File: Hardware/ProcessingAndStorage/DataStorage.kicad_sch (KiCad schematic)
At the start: 10 parts, among them J1 Micro_SD_Card_Det2, U3 LD1117S50TR_SOT223

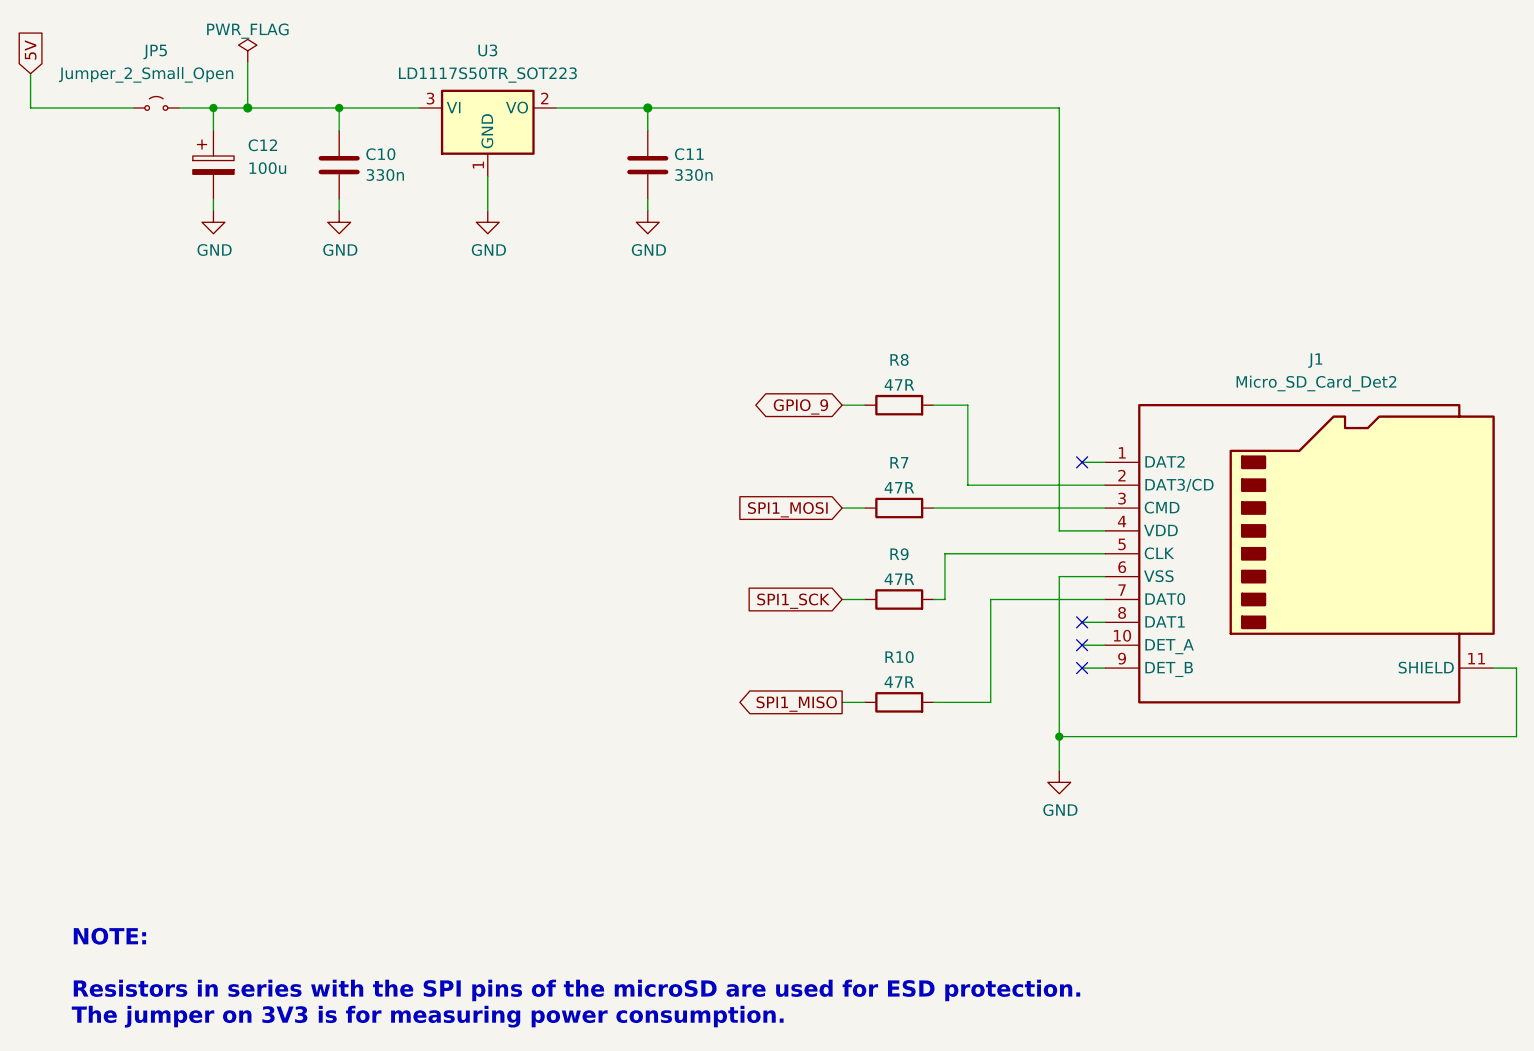
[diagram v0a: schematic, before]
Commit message: make boards smaller, fix sd card slot
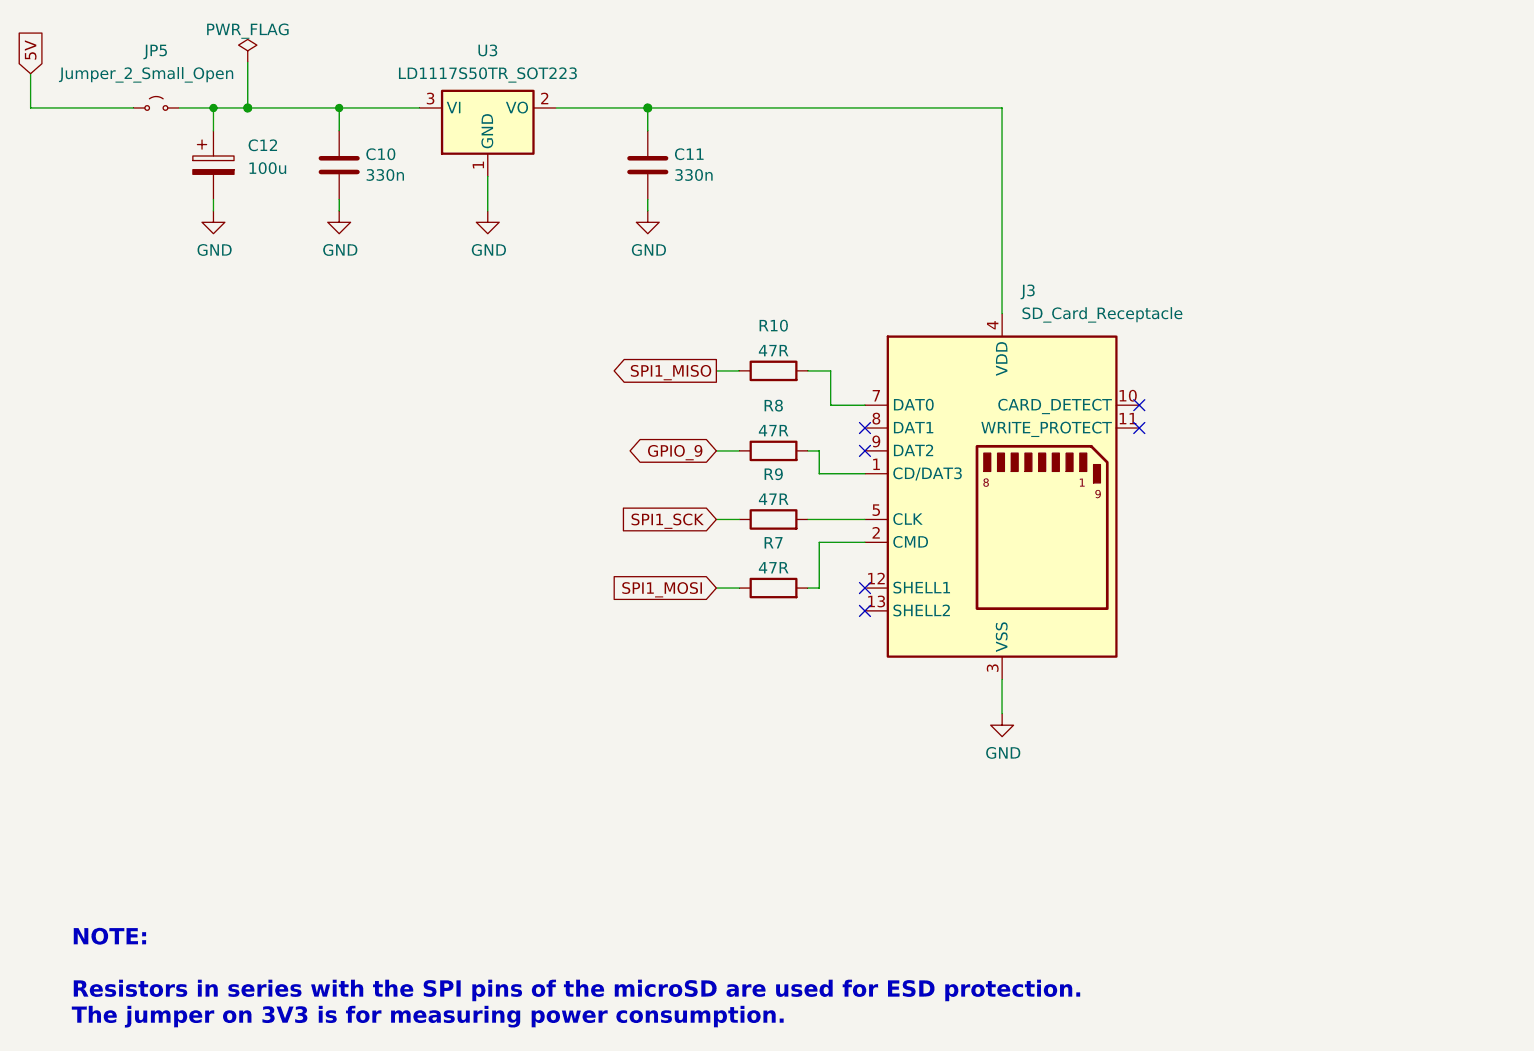
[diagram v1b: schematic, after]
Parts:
- removed J1: Micro_SD_Card_Det2, Connector_Card:SD_TE_2041021, symbol Connector:Micro_SD_Card_Det2
- added J3: SD_Card_Receptacle, symbol Connector:SD_Card_Receptacle
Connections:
- net GND: now also J3.3 (VSS), J3.6 (VSS)
- net at R7.2: now also J3.2 (CMD)
- net at C11.1, U3.2 (VO): now also J3.4 (VDD)
- net at R9.2: now also J3.5 (CLK)
- net at R8.2: now also J3.1 (CD/DAT3)
- net at R10.2: now also J3.7 (DAT0)
- no-connect marks 4 -> 6
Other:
- moved on the sheet: R10, R7, R8, R9

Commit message: make hw
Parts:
- added C13: 330n, Capacitor_SMD:C_0805_2012Metric, symbol Device:C
- J3: footprint (none) -> Connector_Card:SD_TE_2041021
- U3: footprint Package_TO_SOT_SMD:SOT-223 -> Package_TO_SOT_SMD:SOT-223-3_TabPin2
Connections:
- net GND: now also C13.2
- net at C11.1, J3.4 (VDD), U3.2 (VO): now also C13.1
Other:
- moved on the sheet: C10, C11, C12, JP5, U3
